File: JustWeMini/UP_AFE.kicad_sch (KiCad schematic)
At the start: 31 parts, among them U4 ASFLMB-8.000MHZ-LC-T, U5 TDC1000, U6 TDC7200

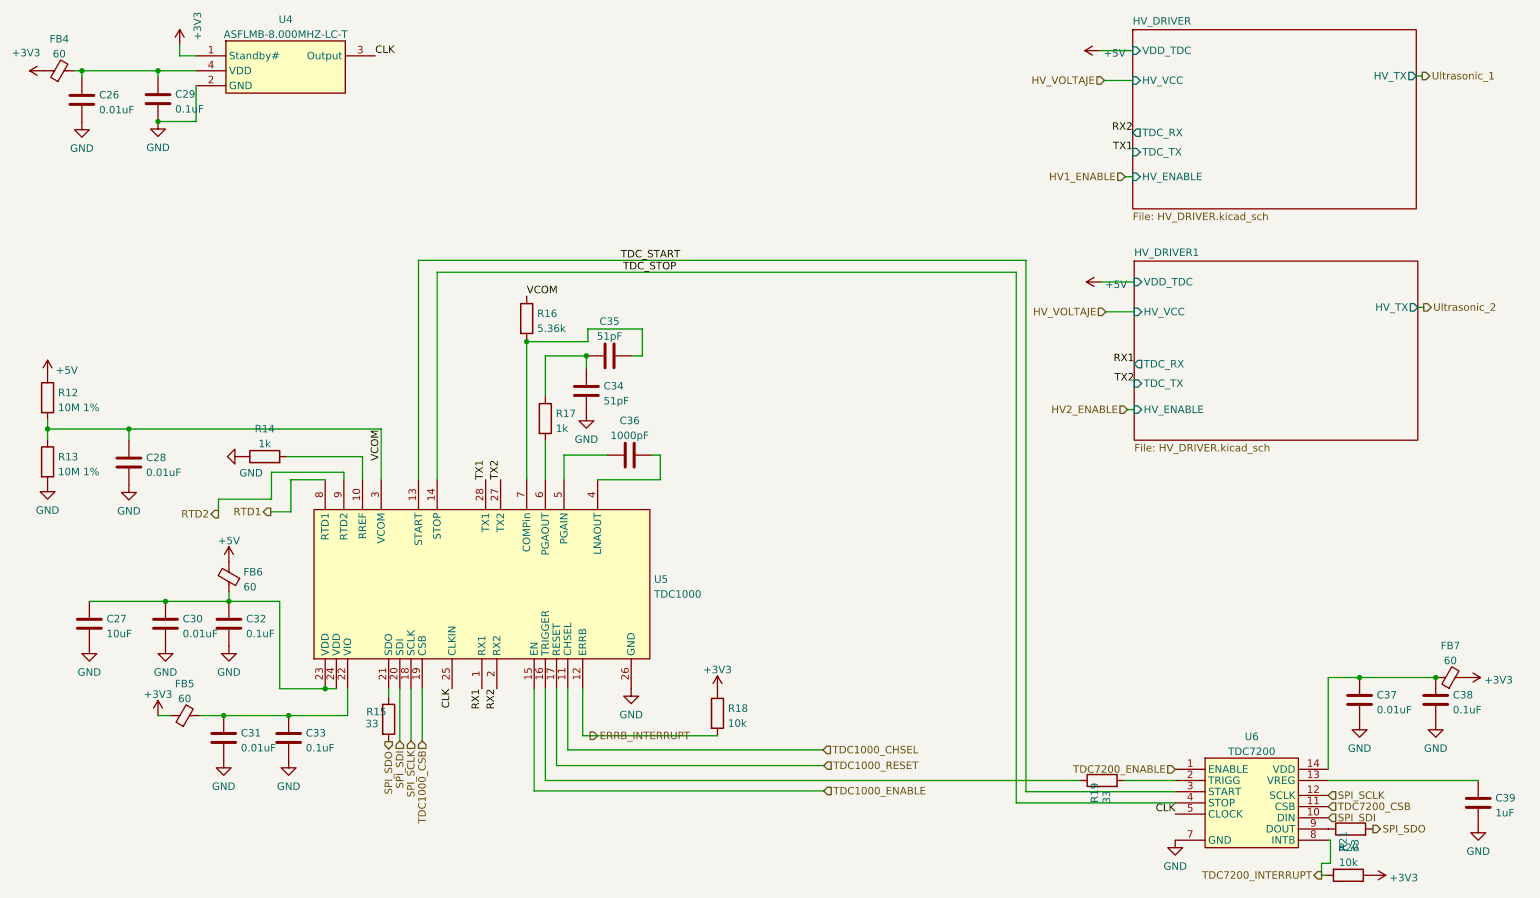
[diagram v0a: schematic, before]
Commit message: Feat: MPN adjusted
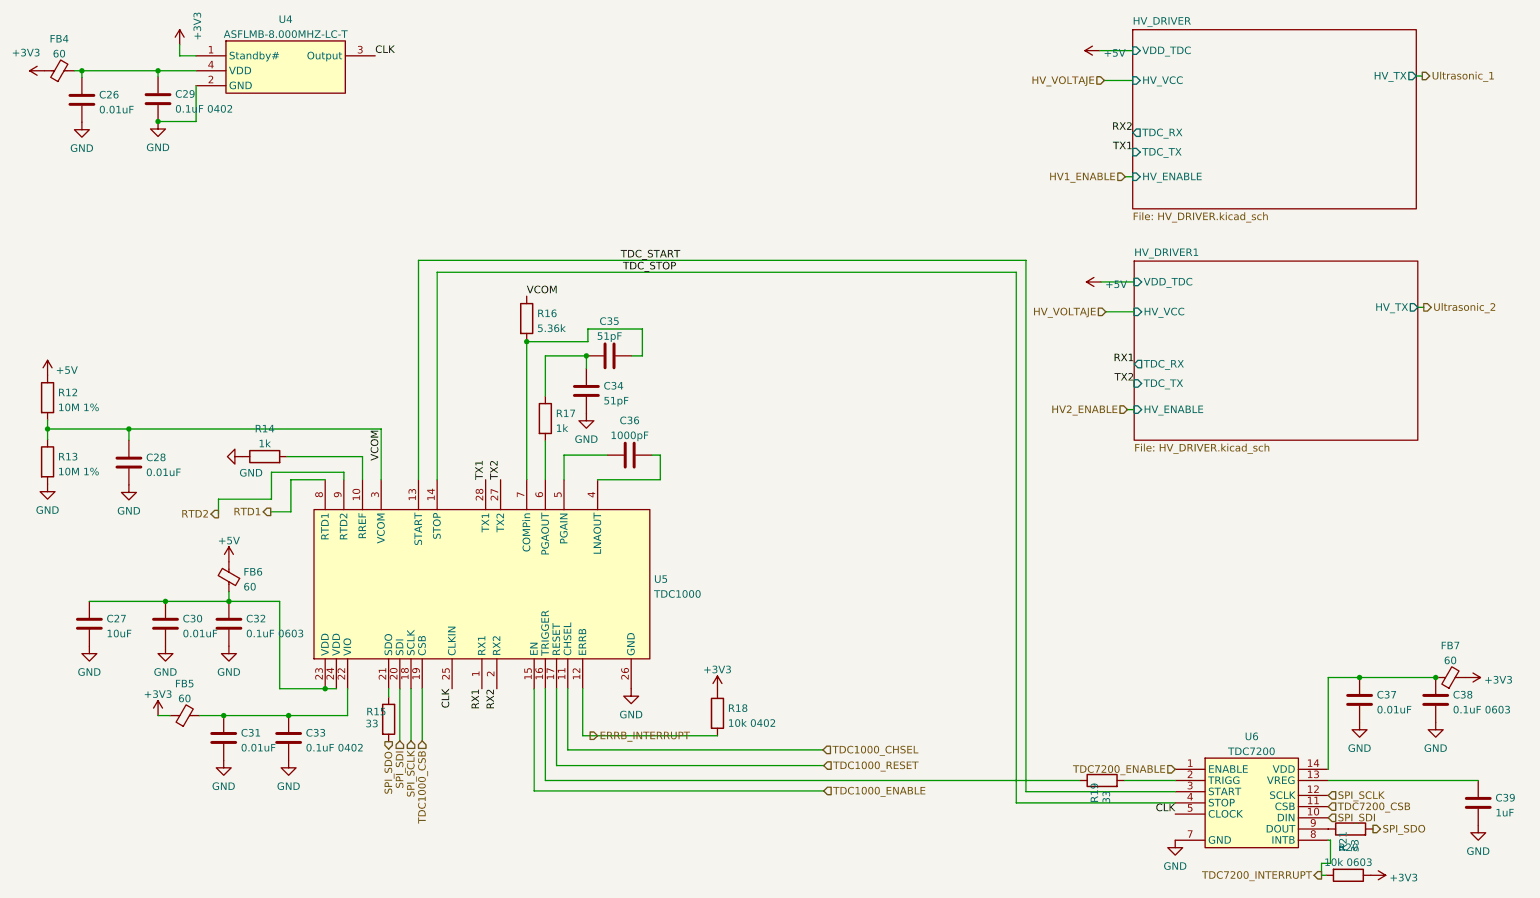
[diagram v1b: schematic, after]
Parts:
- C29, C33: value 0.1uF -> 0.1uF 0402; MPN (none) -> CL05F104ZO5NNND
- C32, C38: value 0.1uF -> 0.1uF 0603
- R18: value 10k -> 10k 0402; MPN (none) -> WR04X1002FTL
- R20: value 10k -> 10k 0603
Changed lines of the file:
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@@
       (effects (font (size 1.27 1.27)) (justify left))
     )
-    (property "Value" "0.1uF" (id 1) (at 266.827 134.7982 0)
+    (property "Value" "0.1uF 0603" (id 1) (at 266.827 134.7982 0)
       (effects (font (size 1.27 1.27)) (justify left))
     )
@@
       (effects (font (size 1.27 1.27)) hide)
     )
-    (property "Datasheet" "~" (id 3) (at 263.906 133.096 0)
+    (property "Datasheet" "" (id 3) (at 263.906 133.096 0)
       (effects (font (size 1.27 1.27)) hide)
     )
@@
       (effects (font (size 1.27 1.27)) hide)
     )
-    (property "Datasheet" "~" (id 3) (at 58.547 112.141 0)
+    (property "Datasheet" "" (id 3) (at 58.547 112.141 0)
       (effects (font (size 1.27 1.27)) hide)
     )
@@
       (effects (font (size 1.27 1.27)) hide)
     )
-    (property "Datasheet" "~" (id 3) (at 249.428 155.067 0)
+    (property "Datasheet" "" (id 3) (at 249.428 155.067 0)
       (effects (font (size 1.27 1.27)) hide)
     )
@@
       (effects (font (size 1.27 1.27)) hide)
     )
-    (property "Datasheet" "~" (id 3) (at 51.054 135.763 0)
+    (property "Datasheet" "" (id 3) (at 51.054 135.763 0)
       (effects (font (size 1.27 1.27)) hide)
     )
@@
       (effects (font (size 1.27 1.27)) hide)
     )
-    (property "Datasheet" "~" (id 3) (at 64.643 91.694 0)
+    (property "Datasheet" "" (id 3) (at 64.643 91.694 0)
       (effects (font (size 1.27 1.27)) hide)
     )
@@
       (effects (font (size 1.27 1.27)) hide)
     )
-    (property "Datasheet" "~" (id 3) (at 34.798 120.142 0)
+    (property "Datasheet" "" (id 3) (at 34.798 120.142 0)
       (effects (font (size 1.27 1.27)) hide)
     )
@@
       (effects (font (size 1.27 1.27)) hide)
     )
-    (property "Datasheet" "~" (id 3) (at 27.686 92.583 0)
+    (property "Datasheet" "" (id 3) (at 27.686 92.583 0)
       (effects (font (size 1.27 1.27)) hide)
     )
@@
       (effects (font (size 1.27 1.27)) hide)
     )
-    (property "Datasheet" "~" (id 3) (at 271.145 150.622 0)
+    (property "Datasheet" "" (id 3) (at 271.145 150.622 0)
       (effects (font (size 1.27 1.27)) hide)
     )
@@
       (effects (font (size 1.27 1.27)) (justify left))
     )
-    (property "Value" "10k" (id 1) (at 143.4612 137.0842 0)
+    (property "Value" "10k 0402" (id 1) (at 143.4612 137.0842 0)
       (effects (font (size 1.27 1.27)) (justify left))
     )
@@
       (effects (font (size 1.27 1.27)) hide)
     )
-    (property "Datasheet" "~" (id 3) (at 141.6832 135.382 0)
-      (effects (font (size 1.27 1.27)) hide)
-    )
-    (property "MPN" "" (id 4) (at 141.6832 135.382 0)
+    (property "Datasheet" "" (id 3) (at 141.6832 135.382 0)
+      (effects (font (size 1.27 1.27)) hide)
+    )
+    (property "MPN" "WR04X1002FTL" (id 4) (at 141.6832 135.382 0)
       (effects (font (size 1.27 1.27)) hide)
     )
@@
       (effects (font (size 1.27 1.27)) hide)
     )
-    (property "Datasheet" "~" (id 3) (at 85.725 136.398 0)
+    (property "Datasheet" "" (id 3) (at 85.725 136.398 0)
       (effects (font (size 1.27 1.27)) hide)
     )
@@
       (effects (font (size 1.27 1.27)) hide)
     )
-    (property "Datasheet" "~" (id 3) (at 47.752 120.142 0)
+    (property "Datasheet" "" (id 3) (at 47.752 120.142 0)
       (effects (font (size 1.27 1.27)) hide)
     )
@@
       (effects (font (size 1.27 1.27)) hide)
     )
-    (property "Datasheet" "~" (id 3) (at 250.952 133.096 0)
+    (property "Datasheet" "" (id 3) (at 250.952 133.096 0)
       (effects (font (size 1.27 1.27)) hide)
     )
@@
       (effects (font (size 1.27 1.27)) hide)
     )
-    (property "Datasheet" "~" (id 3) (at 41.529 92.71 0)
+    (property "Datasheet" "" (id 3) (at 41.529 92.71 0)
       (effects (font (size 1.27 1.27)) hide)
     )
@@
       (effects (font (size 1.27 1.27)) (justify left))
     )
-    (property "Value" "0.1uF" (id 1) (at 71.628 141.2752 0)
+    (property "Value" "0.1uF 0402" (id 1) (at 71.628 141.2752 0)
       (effects (font (size 1.27 1.27)) (justify left))
     )
@@
       (effects (font (size 1.27 1.27)) hide)
     )
-    (property "Datasheet" "~" (id 3) (at 68.707 139.573 0)
-      (effects (font (size 1.27 1.27)) hide)
-    )
-    (property "MPN" "" (id 4) (at 68.707 139.573 0)
+    (property "Datasheet" "" (id 3) (at 68.707 139.573 0)
+      (effects (font (size 1.27 1.27)) hide)
+    )
+    (property "MPN" "CL05F104ZO5NNND" (id 4) (at 68.707 139.573 0)
       (effects (font (size 1.27 1.27)) hide)
     )
@@
       (effects (font (size 1.27 1.27)) hide)
     )
-    (property "Datasheet" "~" (id 3) (at 57.658 139.573 0)
+    (property "Datasheet" "" (id 3) (at 57.658 139.573 0)
       (effects (font (size 1.27 1.27)) hide)
     )
@@
       (effects (font (size 1.27 1.27)) hide)
     )
-    (property "Datasheet" "~" (id 3) (at 27.686 81.661 0)
+    (property "Datasheet" "" (id 3) (at 27.686 81.661 0)
       (effects (font (size 1.27 1.27)) hide)
     )
@@
       (effects (font (size 1.27 1.27)) hide)
     )
-    (property "Datasheet" "~" (id 3) (at 123.317 74.549 0)
+    (property "Datasheet" "" (id 3) (at 123.317 74.549 0)
       (effects (font (size 1.27 1.27)) hide)
     )
@@
       (effects (font (size 1.27 1.27)) hide)
     )
-    (property "Datasheet" "~" (id 3) (at 29.718 26.035 0)
+    (property "Datasheet" "" (id 3) (at 29.718 26.035 0)
       (effects (font (size 1.27 1.27)) hide)
     )
@@
       (effects (font (size 1.27 1.27)) hide)
     )
-    (property "Datasheet" "~" (id 3) (at 33.528 30.988 0)
+    (property "Datasheet" "" (id 3) (at 33.528 30.988 0)
       (effects (font (size 1.27 1.27)) hide)
     )
@@
       (effects (font (size 1.27 1.27)) (justify left))
     )
-    (property "Value" "0.1uF" (id 1) (at 61.468 121.8442 0)
+    (property "Value" "0.1uF 0603" (id 1) (at 61.468 121.8442 0)
       (effects (font (size 1.27 1.27)) (justify left))
     )
@@
       (effects (font (size 1.27 1.27)) hide)
     )
-    (property "Datasheet" "~" (id 3) (at 58.547 120.142 0)
+    (property "Datasheet" "" (id 3) (at 58.547 120.142 0)
       (effects (font (size 1.27 1.27)) hide)
     )
@@
       (effects (font (size 1.27 1.27)) hide)
     )
-    (property "Datasheet" "~" (id 3) (at 126.746 91.44 0)
+    (property "Datasheet" "" (id 3) (at 126.746 91.44 0)
       (effects (font (size 1.27 1.27)) hide)
     )
@@
       (effects (font (size 1.27 1.27)) hide)
     )
-    (property "Datasheet" "~" (id 3) (at 266.446 129.286 0)
+    (property "Datasheet" "" (id 3) (at 266.446 129.286 0)
       (effects (font (size 1.27 1.27)) hide)
     )
@@
       (effects (font (size 1.27 1.27)) hide)
     )
-    (property "Datasheet" "~" (id 3) (at 207.137 146.812 0)
+    (property "Datasheet" "" (id 3) (at 207.137 146.812 0)
       (effects (font (size 1.27 1.27)) hide)
     )
@@
     (in_bom yes) (on_board yes) (fields_autoplaced)
     (property "Reference" "R20" (id 0) (at 249.047 158.2252 90))
-    (property "Value" "10k" (id 1) (at 249.047 160.7621 90))
+    (property "Value" "10k 0603" (id 1) (at 249.047 160.7621 90))
     (property "Footprint" "Resistor_SMD:R_0603_1608Metric" (id 2) (at 249.047 161.163 90)
       (effects (font (size 1.27 1.27)) hide)
     )
-    (property "Datasheet" "~" (id 3) (at 249.047 162.941 0)
+    (property "Datasheet" "" (id 3) (at 249.047 162.941 0)
       (effects (font (size 1.27 1.27)) hide)
     )
@@
       (effects (font (size 1.27 1.27)) hide)
     )
-    (property "Datasheet" "~" (id 3) (at 109.22 68.199 0)
+    (property "Datasheet" "" (id 3) (at 109.22 68.199 0)
       (effects (font (size 1.27 1.27)) hide)
     )
@@
       (effects (font (size 1.27 1.27)) hide)
     )
-    (property "Datasheet" "~" (id 3) (at 112.395 85.217 0)
+    (property "Datasheet" "" (id 3) (at 112.395 85.217 0)
       (effects (font (size 1.27 1.27)) hide)
     )
@@
       (effects (font (size 1.27 1.27)) hide)
     )
-    (property "Datasheet" "~" (id 3) (at 119.38 80.518 0)
+    (property "Datasheet" "" (id 3) (at 119.38 80.518 0)
       (effects (font (size 1.27 1.27)) hide)
     )
@@
       (effects (font (size 1.27 1.27)) (justify left))
     )
-    (property "Value" "0.1uF" (id 1) (at 49.403 32.5632 0)
+    (property "Value" "0.1uF 0402" (id 1) (at 49.403 32.5632 0)
       (effects (font (size 1.27 1.27)) (justify left))
     )
@@
       (effects (font (size 1.27 1.27)) hide)
     )
-    (property "Datasheet" "~" (id 3) (at 46.482 30.861 0)
-      (effects (font (size 1.27 1.27)) hide)
-    )
-    (property "MPN" "" (id 4) (at 46.482 30.861 0)
-      (effects (font (size 1.27 1.27)) hide)
-    )
+    (property "Datasheet" "" (id 3) (at 46.482 30.861 0)
+      (effects (font (size 1.27 1.27)) hide)
+    )
+    (property "MPN" "CL05F104ZO5NNND" (id 4) (at 46.482 30.861 0)
+      (effects (font (size 1.27 1.27)) hide)
+    )
